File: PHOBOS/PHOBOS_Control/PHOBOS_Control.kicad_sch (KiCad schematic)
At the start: 80 parts, among them J1 Screw_Terminal_01x02, J2 Conn_01x06, J3 Conn_Coaxial, J5 DE9_Pins_MountingHoles, J6 USB4056-03-A_REVA2, SW4 KMR211GLFS, U1 SX1280IMLTRT, U2 TLV9351IDCKR, U3 W25Q128JVSIQ, U4 NCP1117-3.3_SOT223, U5 RP2040, U6 TLV9351IDCKR, U7 TLV9351IDCKR, U8 TLV9351IDCKR, Y1 ABM8-272-T3, Y2 C1E-52.000-10-1012-X-M

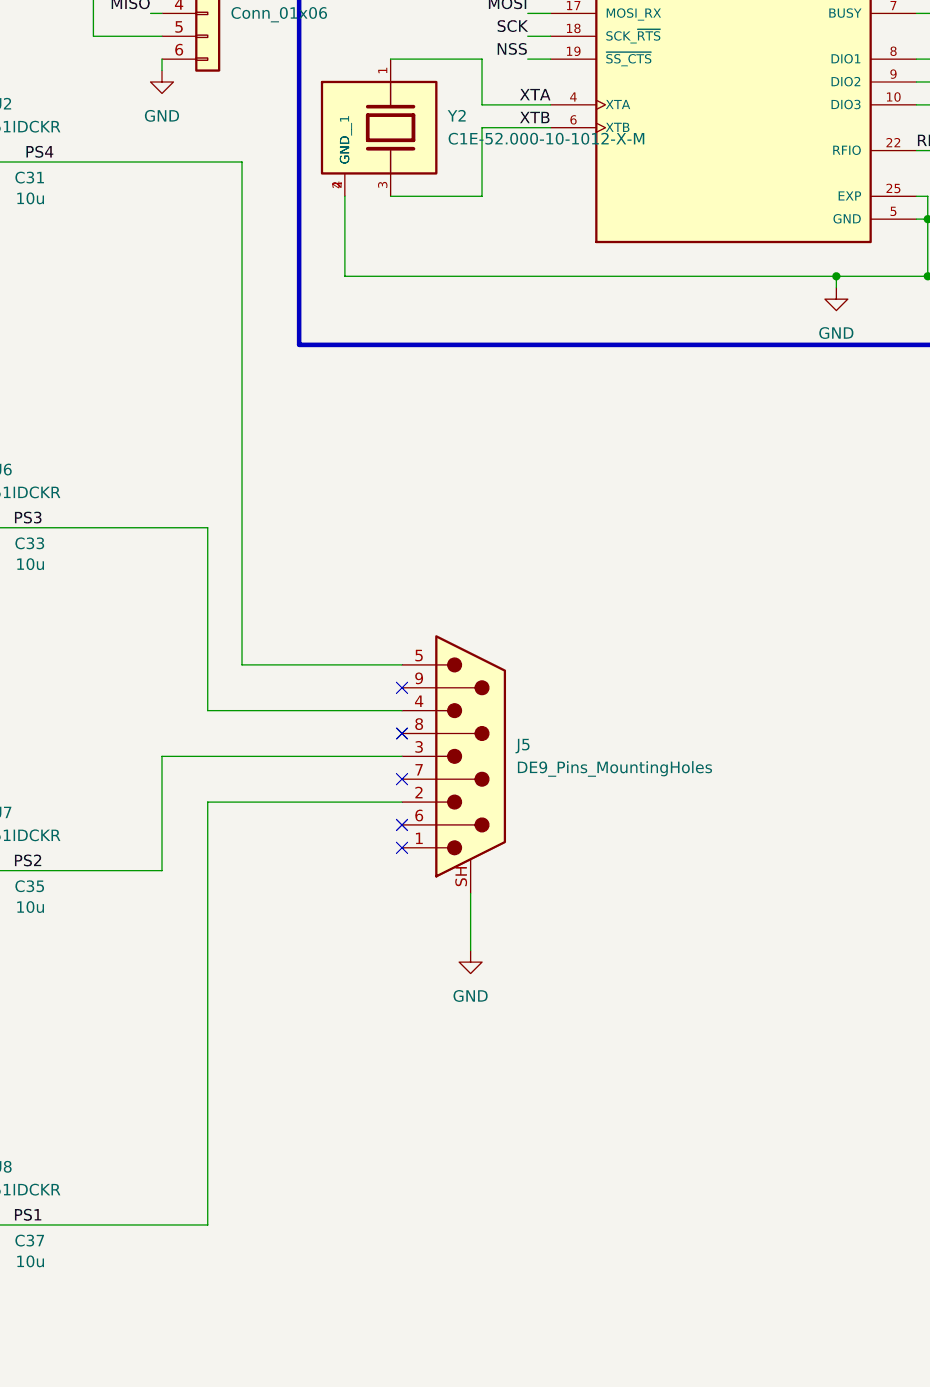
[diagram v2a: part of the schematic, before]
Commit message: repalced with 4-pin connector
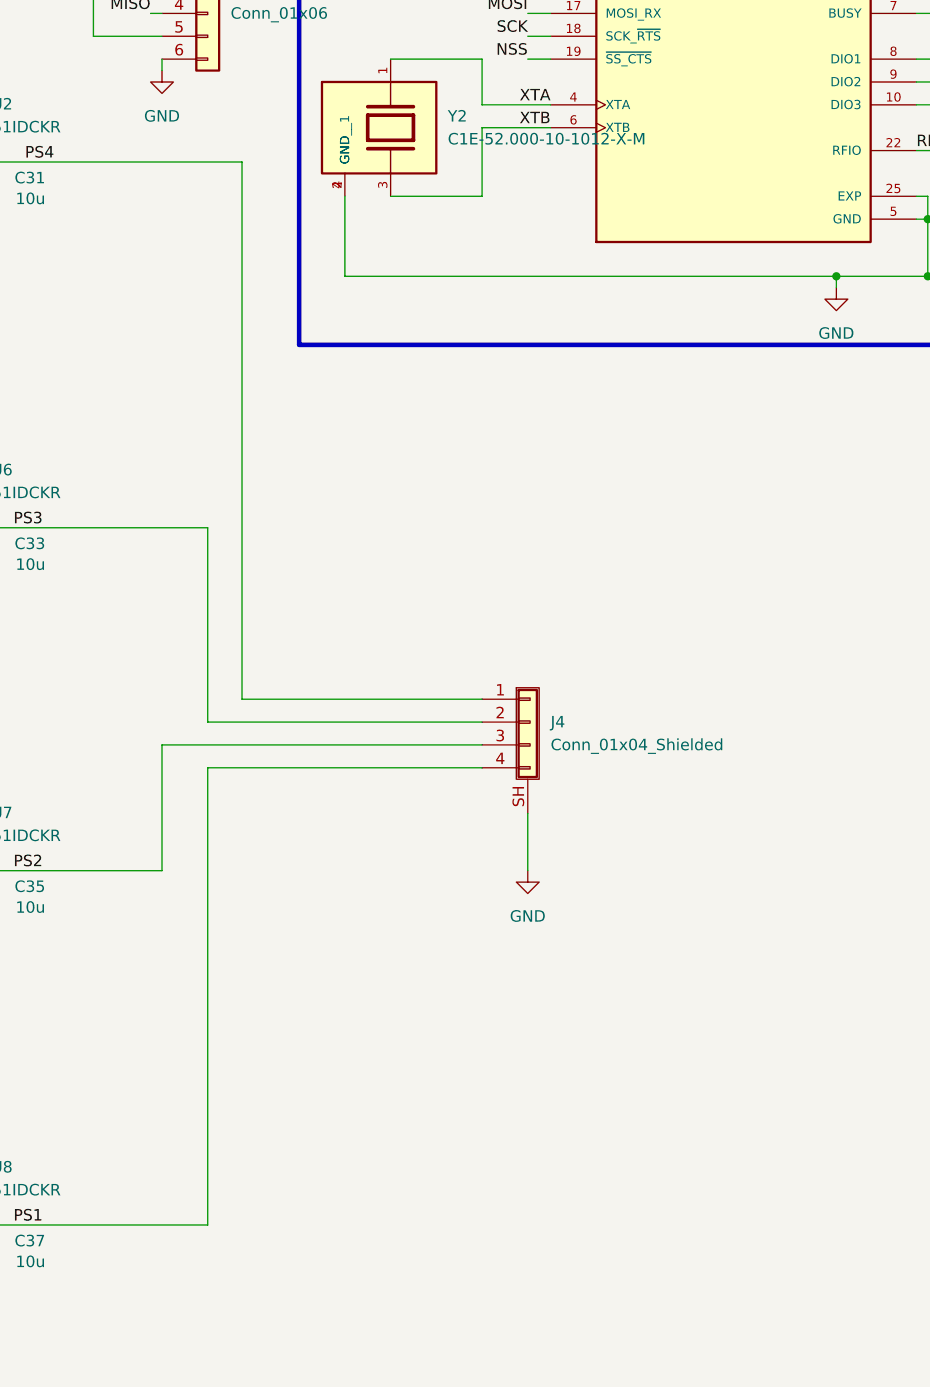
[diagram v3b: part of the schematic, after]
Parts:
- removed J5: DE9_Pins_MountingHoles, Connector_Dsub:DSUB-9_Pins_Horizontal_P2.77x2.84mm_EdgePinOffset7.70mm_Housed_MountingHolesOffset9.12mm, symbol Connector:DE9_Pins_MountingHoles
- added J4: Conn_01x04_Shielded, symbol Connector_Generic_Shielded:Conn_01x04_Shielded
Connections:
- net GND: now also J4.SH (Shield)
- net PS1: now also J4.4 (Pin_4)
- net PS2: now also J4.3 (Pin_3)
- net PS3: now also J4.2 (Pin_2)
- net PS4: now also J4.1 (Pin_1)
- no-connect marks 34 -> 29
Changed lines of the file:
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@@
 	(generator "eeschema")
 	(generator_version "10.0")
-	(paper "A0")
+	(paper "A2")
 	(rectangle
 		(start 205.613 167.513)
@@
 	)
 	(no_connect
-		(at 412.75 303.53)
-	)
-	(no_connect
 		(at 110.49 127)
 	)
@@
 	)
 	(no_connect
-		(at 412.75 308.61)
-	)
-	(no_connect
 		(at 110.49 111.76)
 	)
@@
 	)
 	(no_connect
-		(at 412.75 293.37)
-	)
-	(no_connect
 		(at 429.26 210.82)
 	)
 	(no_connect
-		(at 412.75 298.45)
-	)
-	(no_connect
 		(at 110.49 129.54)
 	)
@@
 	)
 	(no_connect
-		(at 412.75 311.15)
-	)
-	(no_connect
 		(at 318.77 265.43)
 	)
@@
 	(wire
 		(pts
-			(xy 394.97 234.95) (xy 394.97 290.83)
+			(xy 394.97 234.95) (xy 394.97 294.64)
 		)
 		(stroke
@@
 	(wire
 		(pts
-			(xy 391.16 295.91) (xy 412.75 295.91)
+			(xy 391.16 297.18) (xy 421.64 297.18)
 		)
 		(stroke
@@
 	(wire
 		(pts
-			(xy 420.37 316.23) (xy 420.37 322.58)
+			(xy 426.72 307.34) (xy 426.72 313.69)
 		)
 		(stroke
@@
 	(wire
 		(pts
-			(xy 386.08 300.99) (xy 386.08 313.69)
+			(xy 386.08 299.72) (xy 386.08 313.69)
 		)
 		(stroke
@@
 	(wire
 		(pts
-			(xy 394.97 290.83) (xy 412.75 290.83)
+			(xy 394.97 294.64) (xy 421.64 294.64)
 		)
 		(stroke
@@
 	(wire
 		(pts
-			(xy 391.16 353.06) (xy 391.16 306.07)
+			(xy 391.16 353.06) (xy 391.16 302.26)
 		)
 		(stroke
@@
 	(wire
 		(pts
-			(xy 412.75 300.99) (xy 386.08 300.99)
+			(xy 386.08 299.72) (xy 421.64 299.72)
 		)
 		(stroke
@@
 	(wire
 		(pts
-			(xy 391.16 275.59) (xy 391.16 295.91)
+			(xy 391.16 275.59) (xy 391.16 297.18)
 		)
 		(stroke
@@
 	(wire
 		(pts
-			(xy 391.16 306.07) (xy 412.75 306.07)
+			(xy 391.16 302.26) (xy 421.64 302.26)
 		)
 		(stroke
@@
 			(justify left bottom)
 		)
-		(property "Net Class" "PWR"
+		(property "Netclass" "PWR"
 			(at 183.5785 101.6 0)
 			(show_name no)
@@
 			(justify left bottom)
 		)
-		(property "Net Class" "RF"
+		(property "Netclass" "RF"
 			(at 537.9085 231.14 0)
 			(show_name no)
@@
 			(justify left bottom)
 		)
-		(property "Net Class" "RF"
+		(property "Netclass" "RF"
 			(at 525.86 231.14 0)
 			(show_name no)
@@
 			(justify left bottom)
 		)
-		(property "Net Class" "RF"
+		(property "Netclass" "RF"
 			(at 484.5685 231.14 0)
 			(show_name no)
@@
 			(justify left bottom)
 		)
-		(property "Net Class" "RF"
+		(property "Netclass" "RF"
 			(at 508.6985 231.14 0)
 			(show_name no)
@@
 			(justify left bottom)
 		)
-		(property "Net Class" "PWR"
+		(property "Netclass" "PWR"
 			(at 165.7985 101.6 0)
 			(show_name no)
@@
 	)
 	(symbol
-		(lib_id "Connector:DE9_Pins_MountingHoles")
-		(at 420.37 300.99 0)
-		(unit 1)
-		(body_style 1)
-		(exclude_from_sim no)
-		(in_bom yes)
-		(on_board yes)
-		(in_pos_files yes)
-		(dnp no)
-		(property "Reference" "J5"
-			(at 425.45 299.7199 0)
-			(show_name no)
-			(do_not_autoplace no)
-			(effects
-				(font
-					(size 1.27 1.27)
-				)
-				(justify left)
-			)
-		)
-		(property "Value" "DE9_Pins_MountingHoles"
-			(at 425.45 302.2599 0)
-			(show_name no)
-			(do_not_autoplace no)
-			(effects
-				(font
-					(size 1.27 1.27)
-				)
-				(justify left)
-			)
-		)
-		(property "Footprint" "Connector_Dsub:DSUB-9_Pins_Horizontal_P2.77x2.84mm_EdgePinOffset7.70mm_Housed_MountingHolesOffset9.12mm"
-			(at 420.37 300.99 0)
-			(hide yes)
-			(show_name no)
-			(do_not_autoplace no)
-			(effects
-				(font
-					(size 1.27 1.27)
-				)
-			)
-		)
-		(property "Datasheet" ""
-			(at 420.37 300.99 0)
-			(hide yes)
-			(show_name no)
-			(do_not_autoplace no)
-			(effects
-				(font
-					(size 1.27 1.27)
-				)
-			)
-		)
-		(property "Description" "9-pin D-SUB connector, pins (male), Mounting Hole"
-			(at 420.37 300.99 0)
-			(hide yes)
-			(show_name no)
-			(do_not_autoplace no)
-			(effects
-				(font
-					(size 1.27 1.27)
-				)
-			)
-		)
-		(property "MFG #" "6E17C009SAJ120"
-			(at 420.37 300.99 0)
-			(hide yes)
-			(show_name no)
-			(do_not_autoplace no)
-			(effects
-				(font
-					(size 1.27 1.27)
-				)
-			)
-		)
-		(pin "6"
-		)
-		(pin "7"
-		)
-		(pin "SH"
-		)
-		(pin "1"
-		)
-		(pin "2"
-		)
-		(pin "4"
-		)
-		(pin "5"
-		)
-		(pin "8"
-		)
-		(pin "3"
-		)
-		(pin "9"
-		)
-		(instances
-			(project "PHOBOS_Control"
-				(path "/311bc0a8-e09e-4ed9-a164-96f32995a395"
-					(reference "J5")
-					(unit 1)
-				)
-			)
-		)
-	)
-	(symbol
 		(lib_id "Device:L")
 		(at 477.52 213.36 90)
@@
 	(symbol
 		(lib_id "power:GND")
-		(at 420.37 322.58 0)
+		(at 426.72 313.69 0)
 		(unit 1)
 		(body_style 1)
@@
 		(fields_autoplaced yes)
 		(property "Reference" "#PWR035"
-			(at 420.37 328.93 0)
+			(at 426.72 320.04 0)
 			(hide yes)
 			(show_name no)
@@
 		)
 		(property "Value" "GND"
-			(at 420.37 327.66 0)
+			(at 426.72 318.77 0)
 			(show_name no)
 			(do_not_autoplace no)
@@
 		)
 		(property "Footprint" ""
-			(at 420.37 322.58 0)
+			(at 426.72 313.69 0)
 			(hide yes)
 			(show_name no)
@@
 		)
 		(property "Datasheet" ""
-			(at 420.37 322.58 0)
+			(at 426.72 313.69 0)
 			(hide yes)
 			(show_name no)
@@
 		)
 		(property "Description" "Power symbol creates a global label with name \"GND\" , ground"
-			(at 420.37 322.58 0)
+			(at 426.72 313.69 0)
 			(hide yes)
 			(show_name no)
@@
 					(unit 1)
 				)
+			)
+		)
+	)
+	(symbol
+		(lib_id "Connector_Generic_Shielded:Conn_01x04_Shielded")
+		(at 426.72 297.18 0)
+		(unit 1)
+		(body_style 1)
+		(exclude_from_sim no)
+		(in_bom yes)
+		(on_board yes)
+		(in_pos_files yes)
+		(dnp no)
+		(fields_autoplaced yes)
+		(property "Reference" "J4"
+			(at 429.26 297.1799 0)
+			(show_name no)
+			(do_not_autoplace no)
+			(effects
+				(font
+					(size 1.27 1.27)
+				)
+				(justify left)
+			)
+		)
+		(property "Value" "Conn_01x04_Shielded"
+			(at 429.26 299.7199 0)
+			(show_name no)
+			(do_not_autoplace no)
+			(effects
+				(font
+					(size 1.27 1.27)
+				)
+				(justify left)
+			)
+		)
+		(property "Footprint" ""
+			(at 426.72 297.18 0)
+			(hide yes)
+			(show_name no)
+			(do_not_autoplace no)
+			(effects
+				(font
+					(size 1.27 1.27)
+				)
+			)
+		)
+		(property "Datasheet" ""
+			(at 426.72 297.18 0)
+			(hide yes)
+			(show_name no)
+			(do_not_autoplace no)
+			(effects
+				(font
+					(size 1.27 1.27)
+				)
+			)
+		)
+		(property "Description" "Generic shielded connector, single row, 01x04, script generated (kicad-library-utils/schlib/autogen/connector/)"
+			(at 426.72 297.18 0)
+			(hide yes)
+			(show_name no)
+			(do_not_autoplace no)
+			(effects
+				(font
+					(size 1.27 1.27)
+				)
+			)
+		)
+		(pin "3"
+		)
+		(pin "1"
+		)
+		(pin "2"
+		)
+		(pin "SH"
+		)
+		(pin "4"
+		)
+		(instances
+			(project "PHOBOS_Control"
+				(path "/311bc0a8-e09e-4ed9-a164-96f32995a395"
+					(reference "J4")
+					(unit 1)
+				)

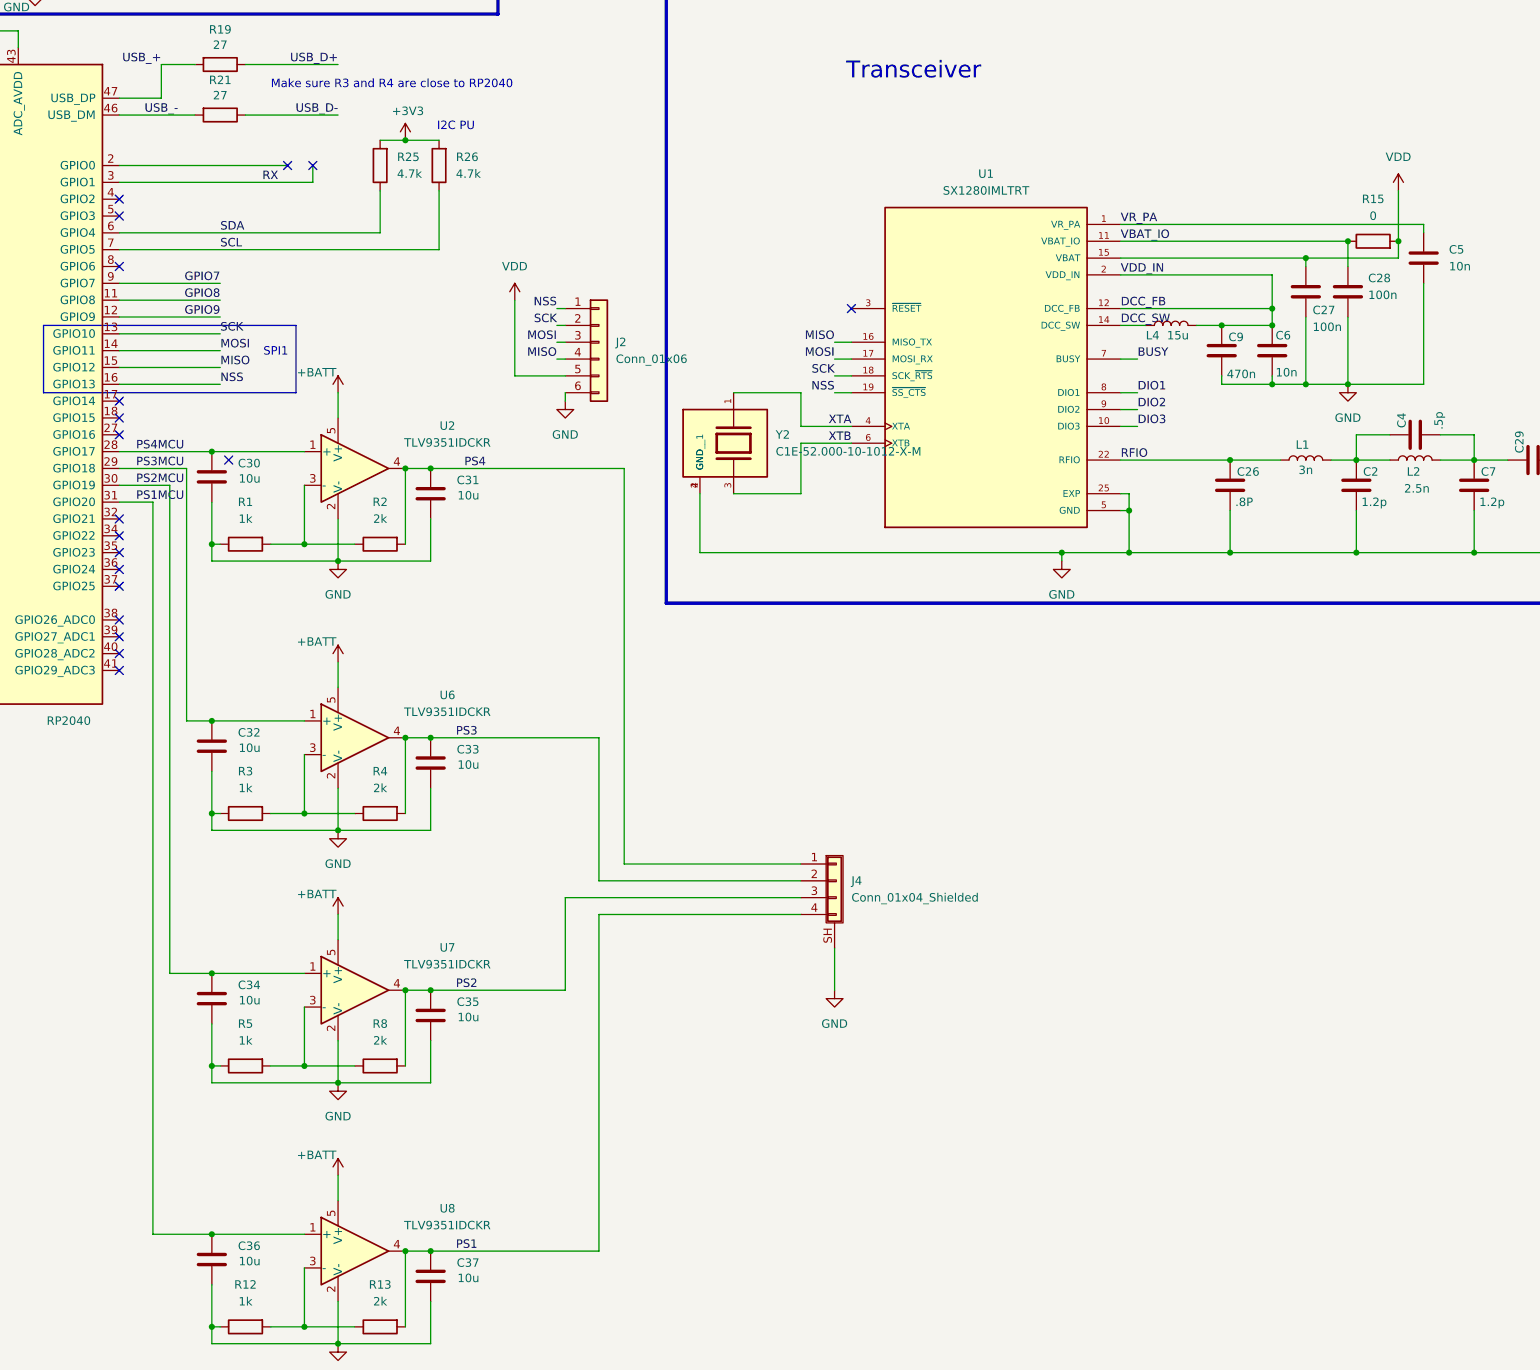
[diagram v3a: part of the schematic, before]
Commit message: design blocks tested. connectors added
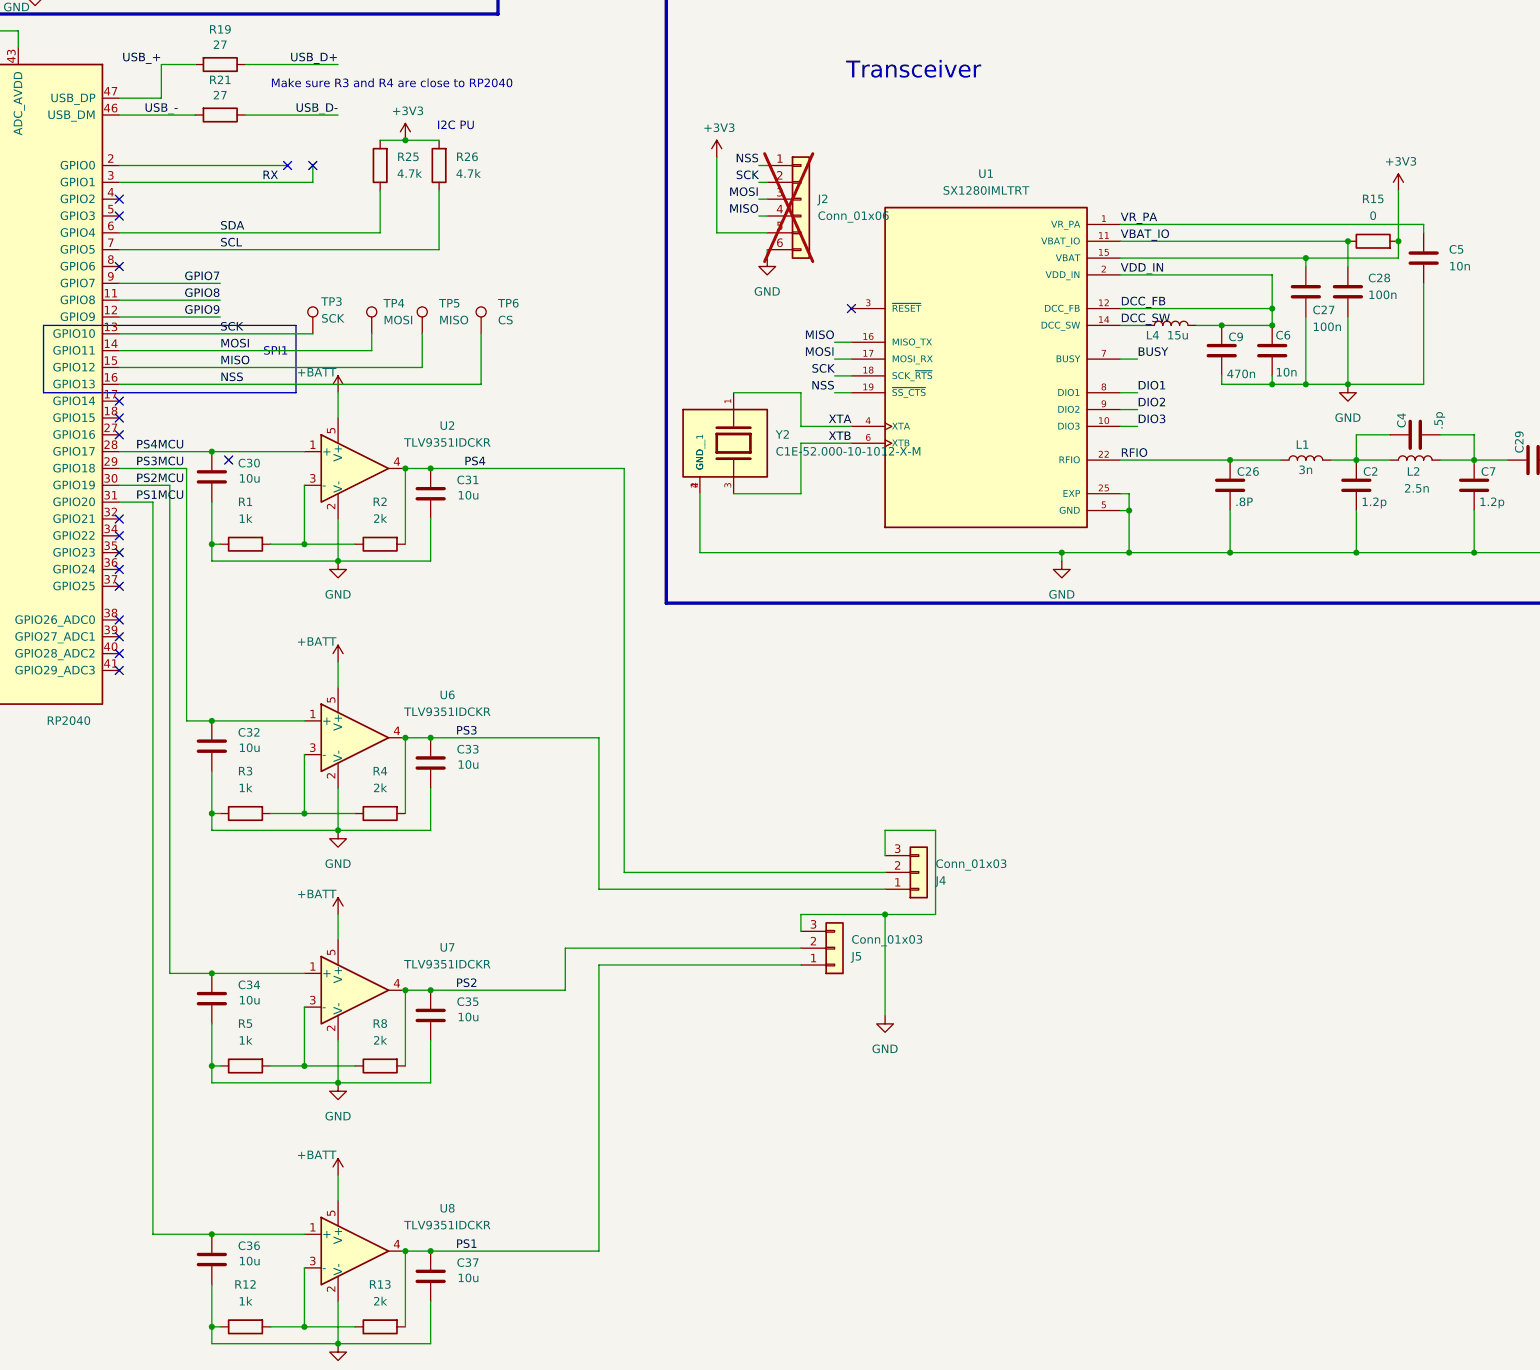
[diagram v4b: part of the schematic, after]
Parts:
- removed J4: Conn_01x04_Shielded, symbol Connector_Generic_Shielded:Conn_01x04_Shielded
- added J4, J5: Conn_01x03, Connector_JST:JST_PH_B3B-PH-K_1x03_P2.00mm_Vertical, symbol Connector_Generic:Conn_01x03
- added TP3: SCK, TestPoint:TestPoint_Plated_Hole_D2.0mm, symbol Connector:TestPoint
- added TP4: MOSI, TestPoint:TestPoint_Plated_Hole_D2.0mm, symbol Connector:TestPoint
- added TP5: MISO, TestPoint:TestPoint_Plated_Hole_D2.0mm, symbol Connector:TestPoint
- added TP6: CS, TestPoint:TestPoint_Plated_Hole_D2.0mm, symbol Connector:TestPoint
- J2: footprint Connector_PinHeader_2.54mm:PinHeader_1x06_P2.54mm_Vertical -> Connector_JST:JST_PH_B6B-PH-K_1x06_P2.00mm_Vertical; now not fitted; now left out of the parts list
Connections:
- net VDD is gone; now on net +3V3: C27.1, J2.5 (Pin_5), R15.2, U1.15 (VBAT)
- net GND: now also J4.3 (Pin_3), J5.3 (Pin_3)
- net MISO: now also TP5.1
- net MOSI: now also TP4.1
- net NSS: now also TP6.1
- net PS1: now also J5.1 (Pin_1)
- net PS2: now also J5.2 (Pin_2)
- net PS3: now also J4.1 (Pin_1)
- net PS4: now also J4.2 (Pin_2)
- net SCK: now also TP3.1
